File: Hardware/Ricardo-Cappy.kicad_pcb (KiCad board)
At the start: 2 copper layers, 56 x 65 mm, 67 parts, among them IC2 AP2205-W5-7, J1 XT60PW-M, J11 Conn_Coaxial, J2 Conn_Coaxial, J3 Conn_02x20_Odd_Even, J4 Conn_01x02_Male, J5 Conn_01x02_Male, J6 Conn_01x02_Male, U1 MAX-M10S, U2 RFM95W-868S2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

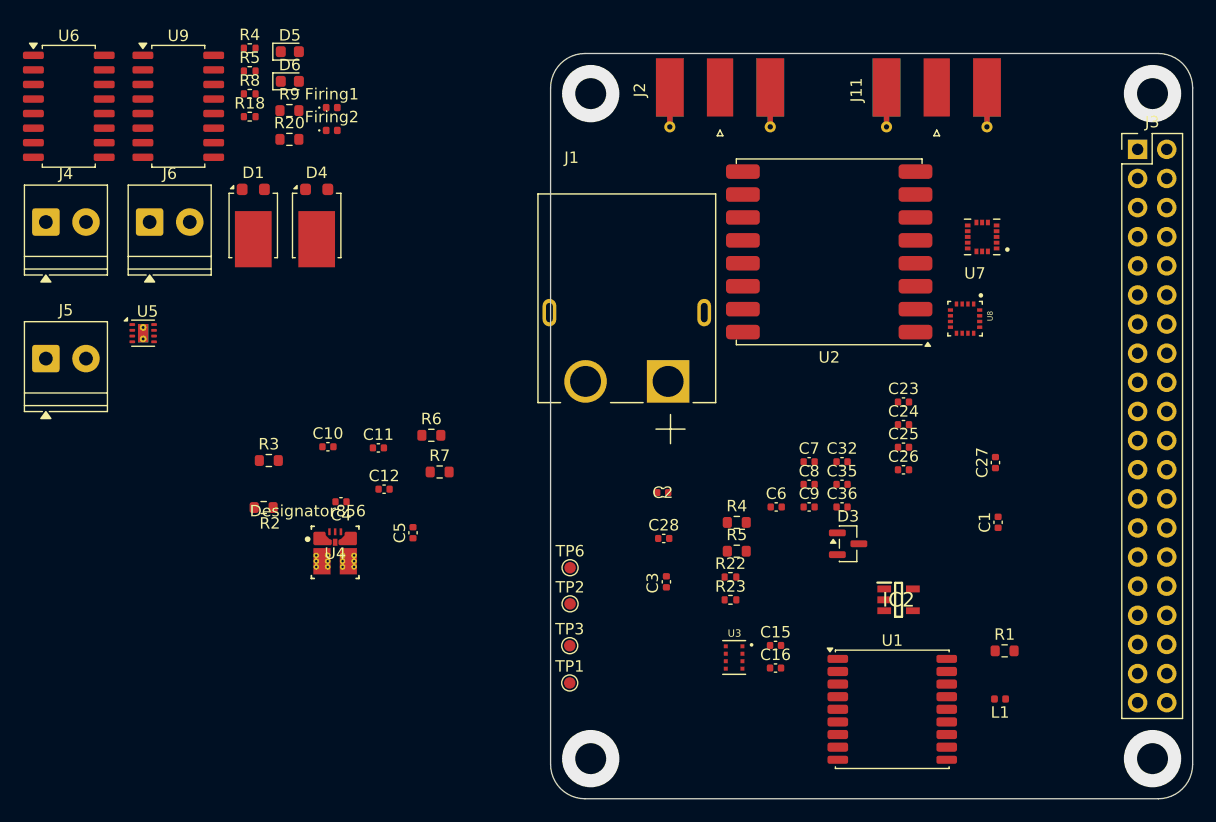
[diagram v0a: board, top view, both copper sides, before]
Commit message: Corrected accidentally deleted connection, reorganised PCB layout (still very WIP)
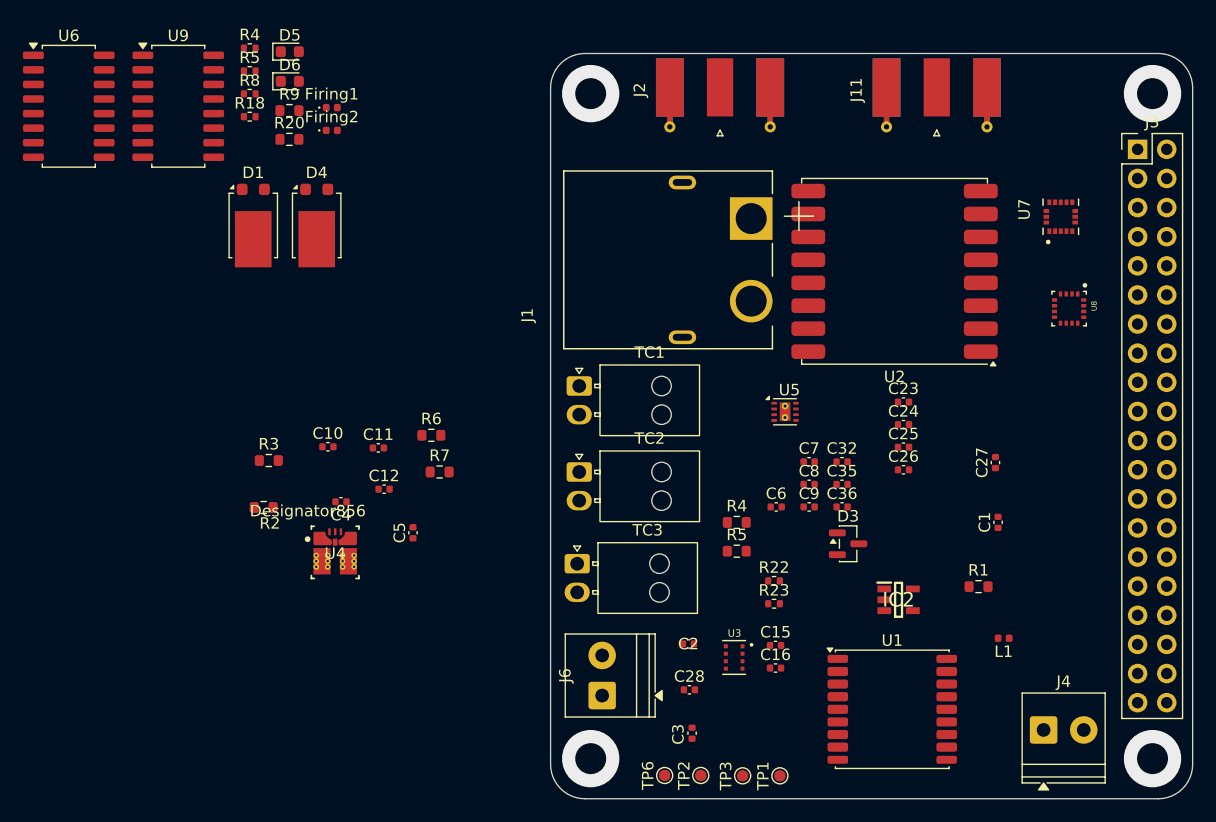
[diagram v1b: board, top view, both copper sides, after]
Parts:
- removed J5: Conn_01x02_Male, TerminalBlock_Phoenix:TerminalBlock_Phoenix_PT-1,5-2-3.5-H_1x02_P3.50mm_Horizontal
- added TC1: Motor Out, Connector_Molex:Molex_Nano-Fit_105313-xx02_1x02_P2.50mm_Horizontal, F.Cu at (134.5, 109.0)
- added TC2: PYRO_1_OUT, Connector_Molex:Molex_Nano-Fit_105313-xx02_1x02_P2.50mm_Horizontal, F.Cu at (134.5, 116.5)
- added TC3: PYRO_2_OUT, Connector_Molex:Molex_Nano-Fit_105313-xx02_1x02_P2.50mm_Horizontal, F.Cu at (134.3, 124.5)
- R2: value 243k -> 226K
- moved J4 97.6 mm to (175.0, 139.0)
- moved J6 57.1 mm to (136.5, 136.0), turned to 90 degrees
- moved U5 56.4 mm to (152.4, 111.2)
- moved TP1 20.0 mm to (152.0, 143.0), turned to 90 degrees
- moved TP6 19.9 mm to (141.9, 143.0), turned to 90 degrees
- moved TP3 18.9 mm to (148.8, 143.0), turned to 90 degrees
- moved TP2 18.8 mm to (145.1, 143.0), turned to 90 degrees
- moved C2 13.4 mm to (144.0, 131.5)
- moved C28 13.4 mm to (144.1, 135.5)
- moved C3 13.4 mm to (144.3, 139.3)
- moved U8 9.12 mm to (177.2, 102.2)
- moved U7 7.08 mm to (176.5, 94.2), turned to 90 degrees
- moved J1 6.68 mm to (143.5, 98.0), turned to 90 degrees
- moved R1 6.04 mm to (169.3, 126.5)
- moved U2 5.95 mm to (162.0, 99.0)
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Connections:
- C4 pad 1: +5.5V -> +5.1V
- C5 pad 1: +5.5V -> +5.1V
- J3 pad 10: unconnected-(J3-Pin_10-Pad10) -> /Nuke 1
- J3 pad 14: unconnected-(J3-Pin_14-Pad14) -> GND
- J3 pad 2: +5V -> +5.1V
- J3 pad 20: unconnected-(J3-Pin_20-Pad20) -> GND
- J3 pad 25: unconnected-(J3-Pin_25-Pad25) -> GND
- J3 pad 28: unconnected-(J3-Pin_28-Pad28) -> /Cont1
- J3 pad 30: unconnected-(J3-Pin_30-Pad30) -> GND
- J3 pad 34: unconnected-(J3-Pin_34-Pad34) -> GND
- J3 pad 35: unconnected-(J3-Pin_35-Pad35) -> /PI_MISO_1
- J3 pad 38: /Cont0 -> /PI_MOSI_1
- J3 pad 39: unconnected-(J3-Pin_39-Pad39) -> GND
- J3 pad 4: unconnected-(J3-Pin_4-Pad4) -> +5.1V
- J3 pad 40: /Nuke 1 -> /PI_SCLK_1
- J3 pad 8: unconnected-(J3-Pin_8-Pad8) -> /Cont0
- J3 pad 9: unconnected-(J3-Pin_9-Pad9) -> GND
- R2 pad 1: +5.5V -> +5.1V
- R9 pad 1: /Cont0 -> /Cont1
- U3 pad 3: /PI_MOSI -> /PI_MOSI_1
- U3 pad 4: /PI_SCLK -> /PI_SCLK_1
- U3 pad 5: /PI_MISO -> /PI_MISO_1
- U4 pad 3: +5.5V -> +5.1V
- U5 pad 1: +5.5V -> +5.1V
- U5 pad 8: +5V -> +3V3
- U9 pad 9: /Cont0 -> /Cont1
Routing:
- net Net-(D2-A): vias 0 -> 1
- net (no net): vias 4 -> 3
